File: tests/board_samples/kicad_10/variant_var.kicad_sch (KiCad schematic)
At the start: 0 parts

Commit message: [KiCad 10][Added] Support to native variants on KiAuto targets
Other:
- title: (none) -> ${VARIANT}
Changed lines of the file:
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@@
 	(generator_version "10.0")
 	(paper "A4")
+	(title_block
+		(title "${VARIANT}")
+		(comment 1 "${VARIANT_DESC}")
+	)
 	(text "${VARIANT_DESC}"
 		(exclude_from_sim no)
@@
 	)
 	(embedded_fonts no)
+	(embedded_files
+		(file
+			(name "kicad_embedded_F47E35086DF2D1FFFBB7A2664A356353.kicad_wks")
+			(type worksheet)
+			(data |KLUv/WA5CfUUANbdXiEAtxsWHGS5ac4JWlhdTV1ADhVltCCdFsc54zb0/38BIAJVAE0AWQCPPxL/
+				x2PzpH2tJ3sj5zsuFjBqzf58aEl+rVjALNp+suWX/AkAQIAUvZfTYlScKuO3oXNEsuqM38t+3UMA
+				BAoLSulVZ+2LbZl9RAAEyhCJE3qgDRECf3GHNla7xGRFq/6S//fYvLDaEzOVMnjte056zn4zBl/s
+				2bMKgVj82sW33/75Dq8IZ6+r/uvjiMHatcPriKsnpf3Z+7Kq2kfvPuh5xB+Xk+VCEX+NqBXLxm0a
+				DTNyzGJRtYRaiGZM6uC0B6cNneoq2YbJNKgBZmE9KWVYiVYsUlqXPThahuM21KAb/t4j52zK/tfB
+				NnXslyIQVptmpor1/L5v0gsQCIFComKMq16Iyrhoos6LdhWNYroeOWLHrJtKdqFYHIpIl106TYtw
+				i8VlIShZRZtsEAsBrei9bYU1qTbptk5821Ua2n73Dyc4pAThVvV7Y8adzk56F4x2yQKAgKARQYYU
+				mhopSFLIMAeARKTmqDqUaDDAcOWIIIoJCEAecpszKGXvooqHvkhFQiG28uvJM4eHQAh+709Se2SN
+				7fZmG2qbN/1QC5OEnj8ZW3lkLDPwAUK2Oq0TU672a4nDEjmEFWhklqn0WFP67FIvkQYbw2kO4q6/
+				qnWHAldYseSqixd3LE/J8NeCQI9DAc/eEQ56ASaz3qSVl0iGfyoHi20cwRsYNqCHjWUKPgIRIRMZ
+				ml8MJWGBXuZN8Fk8JDGNHD6J7nSKOp9OnHub7M4WY9jDfxY4UCDLPHrUDohbmNiJcBAR7RFexSHX
+				AgS3v8mzU7ToWk28KOCM2sWSXyLaQydtQvsmK0YepdjxERvjpVJ6VyjsER/x3hc6hGF89Co=|
+			)
+			(checksum "F47E35086DF2D1FFFBB7A2664A356353")
+		)
+	)
 )

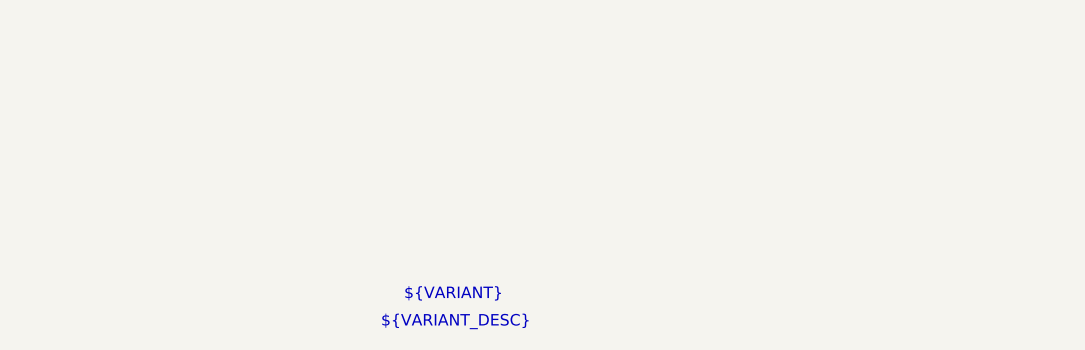
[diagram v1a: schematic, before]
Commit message: [Tests][Added][KiCad 10] Native variants schematic print
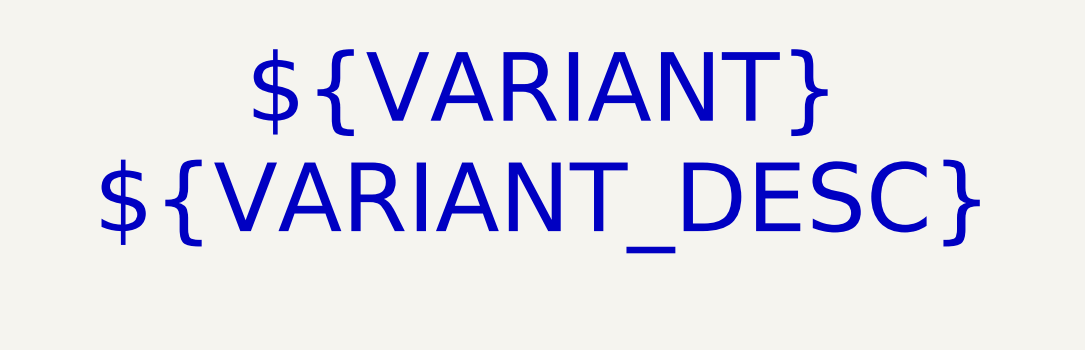
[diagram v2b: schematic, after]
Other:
- note added: "${VARIANT} ${VARIANT_DESC}"
- note removed: "${VARIANT_DESC}"
- note removed: "${VARIANT}"
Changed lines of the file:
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@@
 		(title "${VARIANT}")
 		(comment 1 "${VARIANT_DESC}")
+		(comment 2 "${VARIANT}")
 	)
-	(text "${VARIANT_DESC}"
+	(text "${VARIANT}\n${VARIANT_DESC}"
 		(exclude_from_sim no)
-		(at 93.472 63.754 0)
+		(at 103.124 44.196 0)
 		(effects
 			(font
-				(size 1.27 1.27)
+				(size 7.62 7.62)
 			)
 		)
-	)
-	(text "${VARIANT}"
-		(exclude_from_sim no)
-		(at 93.218 60.706 0)
-		(effects
-			(font
-				(size 1.27 1.27)
-			)
-		)
